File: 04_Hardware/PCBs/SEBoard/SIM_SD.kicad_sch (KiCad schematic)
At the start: 40 parts, among them IC2 ST4SI2M0020TPIFW, J16 SIM8066-6-1-14-01-A, J17 MEM2067-02-180-00-A, U1 SC200EEMNA-E53-UGNDA

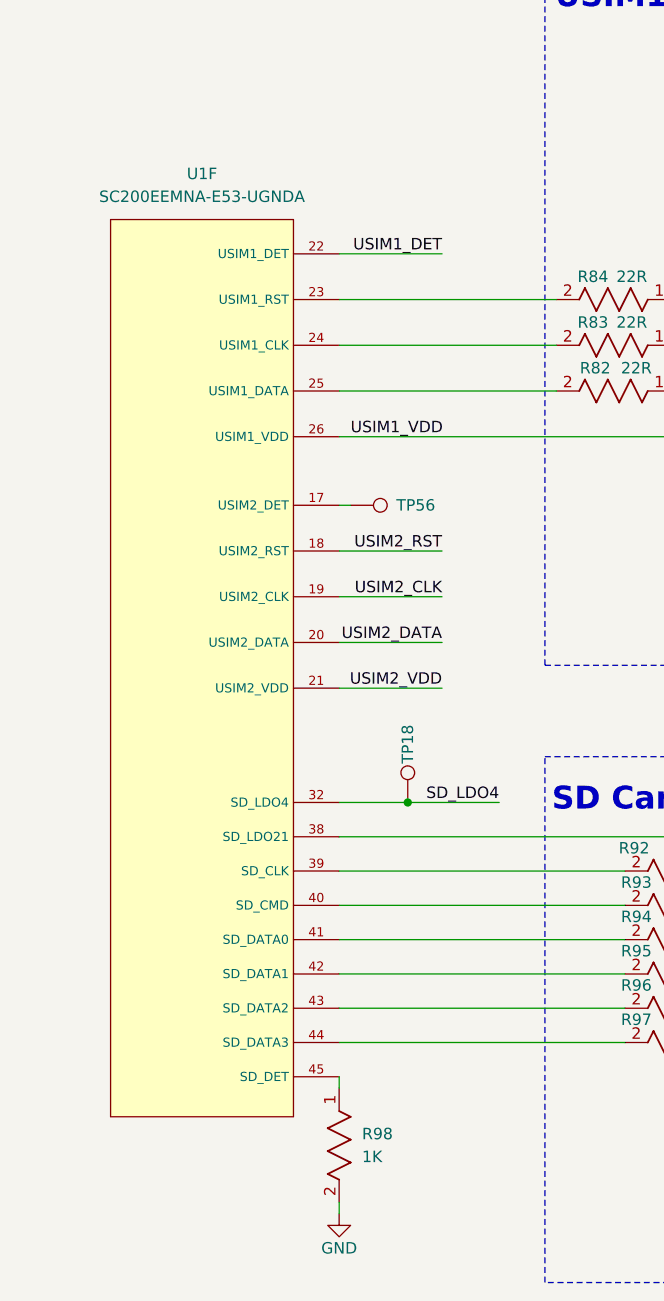
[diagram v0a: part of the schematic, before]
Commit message: feat(schematic): add SE250B4 symbol to schematic (unchecked)
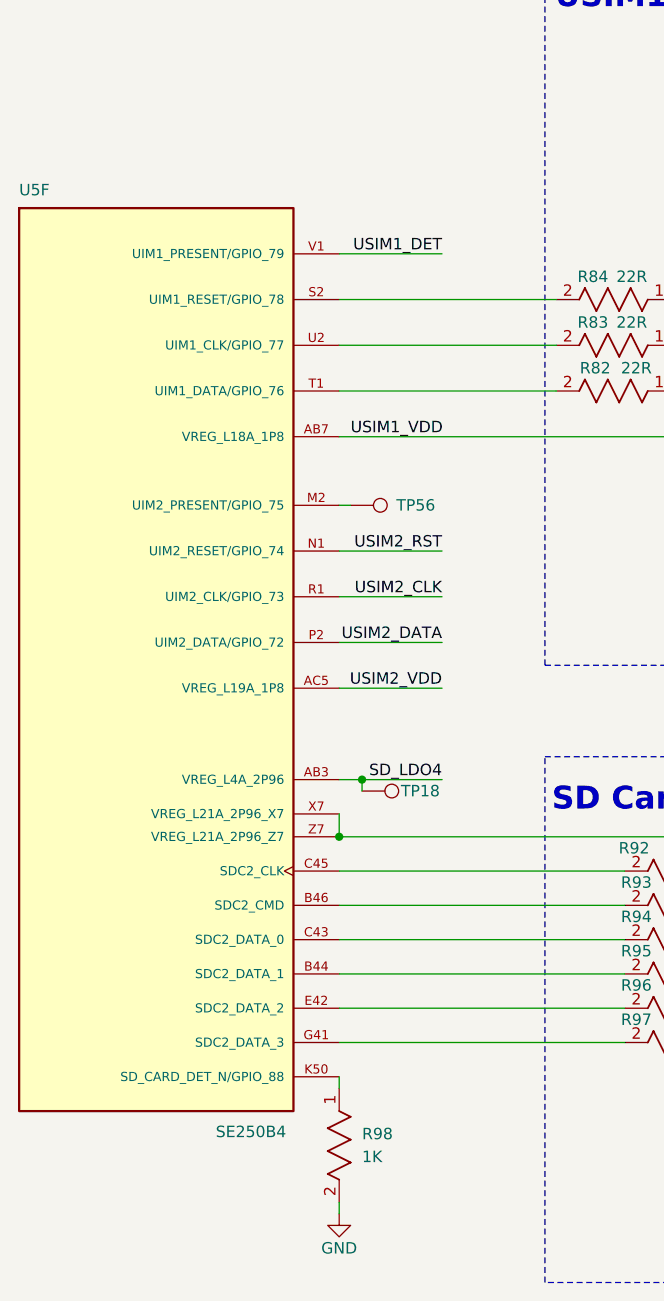
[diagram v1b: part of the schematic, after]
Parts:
- removed U1: SC200EEMNA-E53-UGNDA, SEBoard:SC200E_SC206E, symbol SEBoard:SC200E
- added U5: SE250B4, 000MCLib:XCVR_SE250B4-NA, symbol 000MCLib:SE250B4
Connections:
- net SD_LDO4: now also U5.AB3 (VREG_L4A_2P96)
- net USIM1_DET: now also U5.V1 (UIM1_PRESENT/GPIO_79)
- net USIM1_VDD: now also U5.AB7 (VREG_L18A_1P8)
- net USIM2_CLK: now also U5.R1 (UIM2_CLK/GPIO_73)
- net USIM2_DATA: now also U5.P2 (UIM2_DATA/GPIO_72)
- net USIM2_RST: now also U5.N1 (UIM2_RESET/GPIO_74)
- net USIM2_VDD: now also U5.AC5 (VREG_L19A_1P8)
- net at R93.2: now also U5.B46 (SDC2_CMD)
- net at R95.2: now also U5.B44 (SDC2_DATA_1)
- net at R92.2: now also U5.C45 (SDC2_CLK)
- net at R82.2: now also U5.T1 (UIM1_DATA/GPIO_76)
- net at R94.2: now also U5.C43 (SDC2_DATA_0)
- net at R97.2: now also U5.G41 (SDC2_DATA_3)
- net at C88.1, C89.1, D21.1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: now also U5.X7 (VREG_L21A_2P96_X7), U5.Z7 (VREG_L21A_2P96_Z7)
- net at TP56.1: now also U5.M2 (UIM2_PRESENT/GPIO_75)
- net at R84.2: now also U5.S2 (UIM1_RESET/GPIO_78)
- net at R96.2: now also U5.E42 (SDC2_DATA_2)
- net at R83.2: now also U5.U2 (UIM1_CLK/GPIO_77)
- net at R98.1: now also U5.K50 (SD_CARD_DET_N/GPIO_88)
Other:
- moved on the sheet: TP18

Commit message: feat: Updated schematic layout and moved new components to Layout
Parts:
- C81, C82, C83, C85, C86, C87: footprint SEBoard:CAPC1005X55N -> 000MCLib:CAPC1005X55N; symbol SEBoard:GRM1555C1H220JA01D -> 000MCLib:GRM1555C1H220JA01D
- C84: footprint SEBoard:CAPC1005X55N -> 000MCLib:CAPC1005X55N; symbol SEBoard:GRM155R71A104KA01D -> 000MCLib:GRM155R71A104KA01D
- C88: footprint SEBoard:GRM31x -> 000MCLib:GRM31x; symbol SEBoard:GRM31CR60J476ME19L -> 000MCLib:GRM31CR60J476ME19L
- C89: footprint SEBoard:CAPC1005X55N -> 000MCLib:CAPC1005X55N; symbol SEBoard:GRM1555C1H330JA01D -> 000MCLib:GRM1555C1H330JA01D
- D20: footprint SEBoard:SOT95P280X145-6N -> 000MCLib:SOT95P280X145-6N; symbol SEBoard:SRV05-4.TCT -> 000MCLib:SRV05-4.TCT
- D21, D22, D23, D24, D25, D26, D27: footprint SEBoard:SC120501ETG -> 000MCLib:SC120501ETG; symbol SEBoard:SC1205-01ETG -> 000MCLib:SC1205-01ETG
- IC2: footprint SON127P600X500X100-9N -> 000MCLib:SON127P600X500X100-9N; symbol SEBoard:ST4SI2M0020TPIFW -> 000MCLib:ST4SI2M0020TPIFW
- J16: footprint SEBoard:SIM8066611401A -> 000MCLib:SIM8066611401A; symbol SEBoard:SIM8066-6-1-14-01-A -> 000MCLib:SIM8066-6-1-14-01-A
- J17: footprint SEBoard:MEM20670218000A -> 000MCLib:MEM20670218000A; symbol SEBoard:MEM2067-02-180-00-A -> 000MCLib:MEM2067-02-180-00-A
- R82, R83, R84, R87, R89, R90: footprint SEBoard:RC0402N_YAG -> 000MCLib:RC0402N_YAG; symbol SEBoard:RC0402JR-0722RL -> 000MCLib:RC0402JR-0722RL
- R85: footprint SEBoard:RC0402N_YAG -> 000MCLib:RC0402N_YAG; symbol SEBoard:RC0402JR-07100KL -> 000MCLib:RC0402JR-07100KL
- R86, R91: footprint SEBoard:RC0402N_YAG -> 000MCLib:RC0402N_YAG; symbol SEBoard:RC0402JR-0710KL -> 000MCLib:RC0402JR-0710KL
- R88: footprint SEBoard:RC0402N_YAG -> 000MCLib:RC0402N_YAG; symbol SEBoard:RC0402JR-070RL -> 000MCLib:RC0402JR-070RL
- R92, R93, R94, R95, R96, R97: footprint SEBoard:RC0402N_YAG -> 000MCLib:RC0402N_YAG; symbol SEBoard:RC0402JR-0733RL -> 000MCLib:RC0402JR-0733RL
- R98: footprint SEBoard:RC0402N_YAG -> 000MCLib:RC0402N_YAG; symbol SEBoard:RC0402JR-071KL -> 000MCLib:RC0402JR-071KL
- TP18, TP56: symbol SEBoard:TestPoint -> 000MCLib:TestPoint
